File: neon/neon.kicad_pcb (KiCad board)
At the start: 2 copper layers, 42 parts, among them J1 VBUS-VCC, J2 V3V3-GND, J3 V3V3-GND, J4 V3V3-GND, J5 V3V3-VIO, Q1 BC807, Q2 BC807, Q3 BC807, Q4 BC807, Q5 BC807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

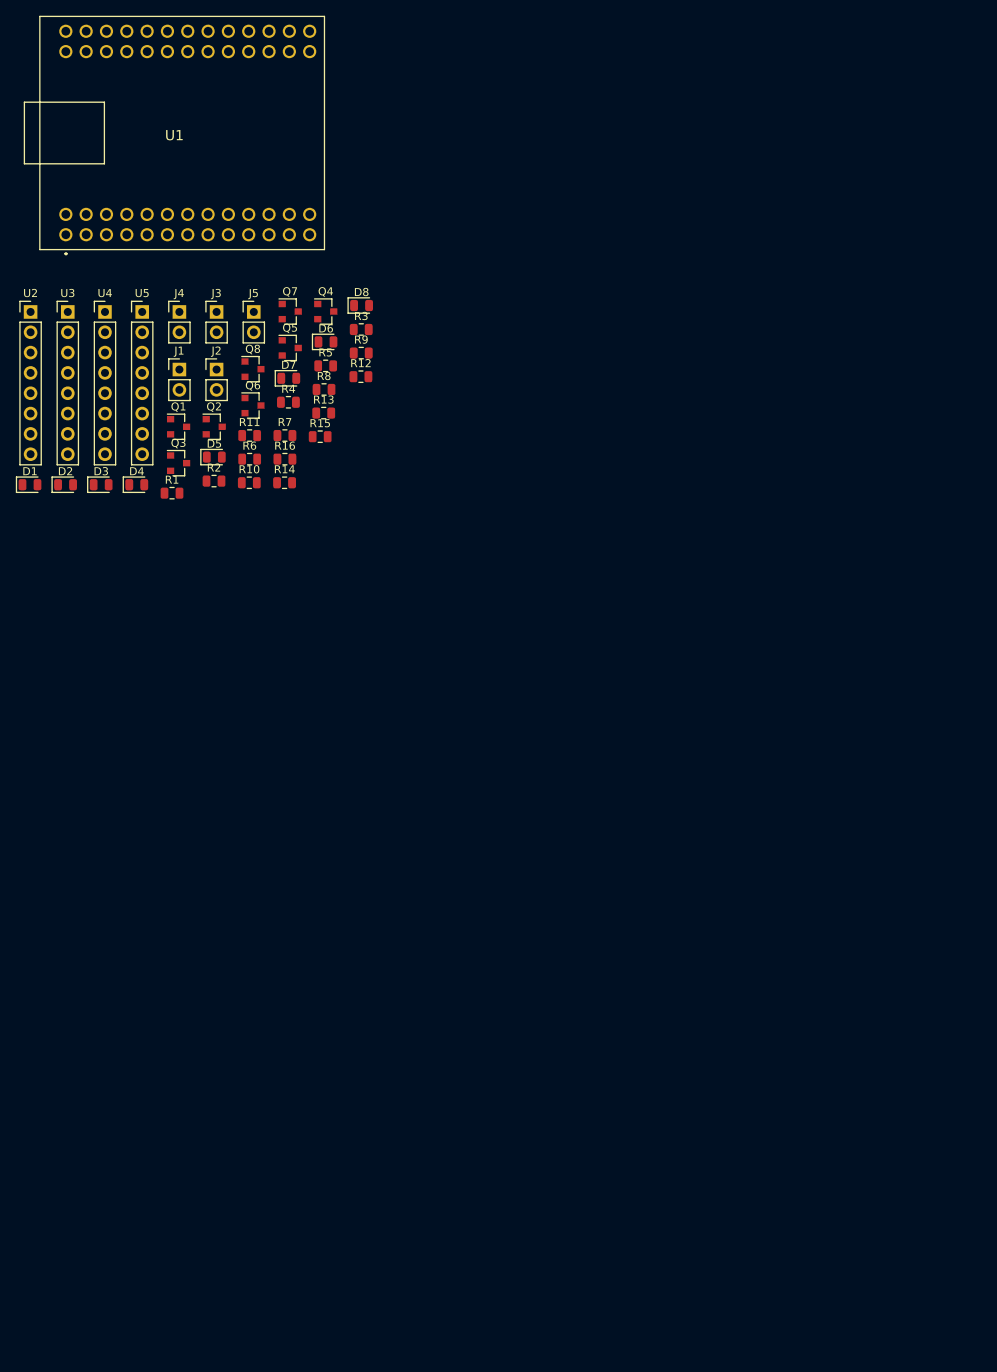
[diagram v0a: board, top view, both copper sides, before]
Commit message: Order pins on footprint - part 1
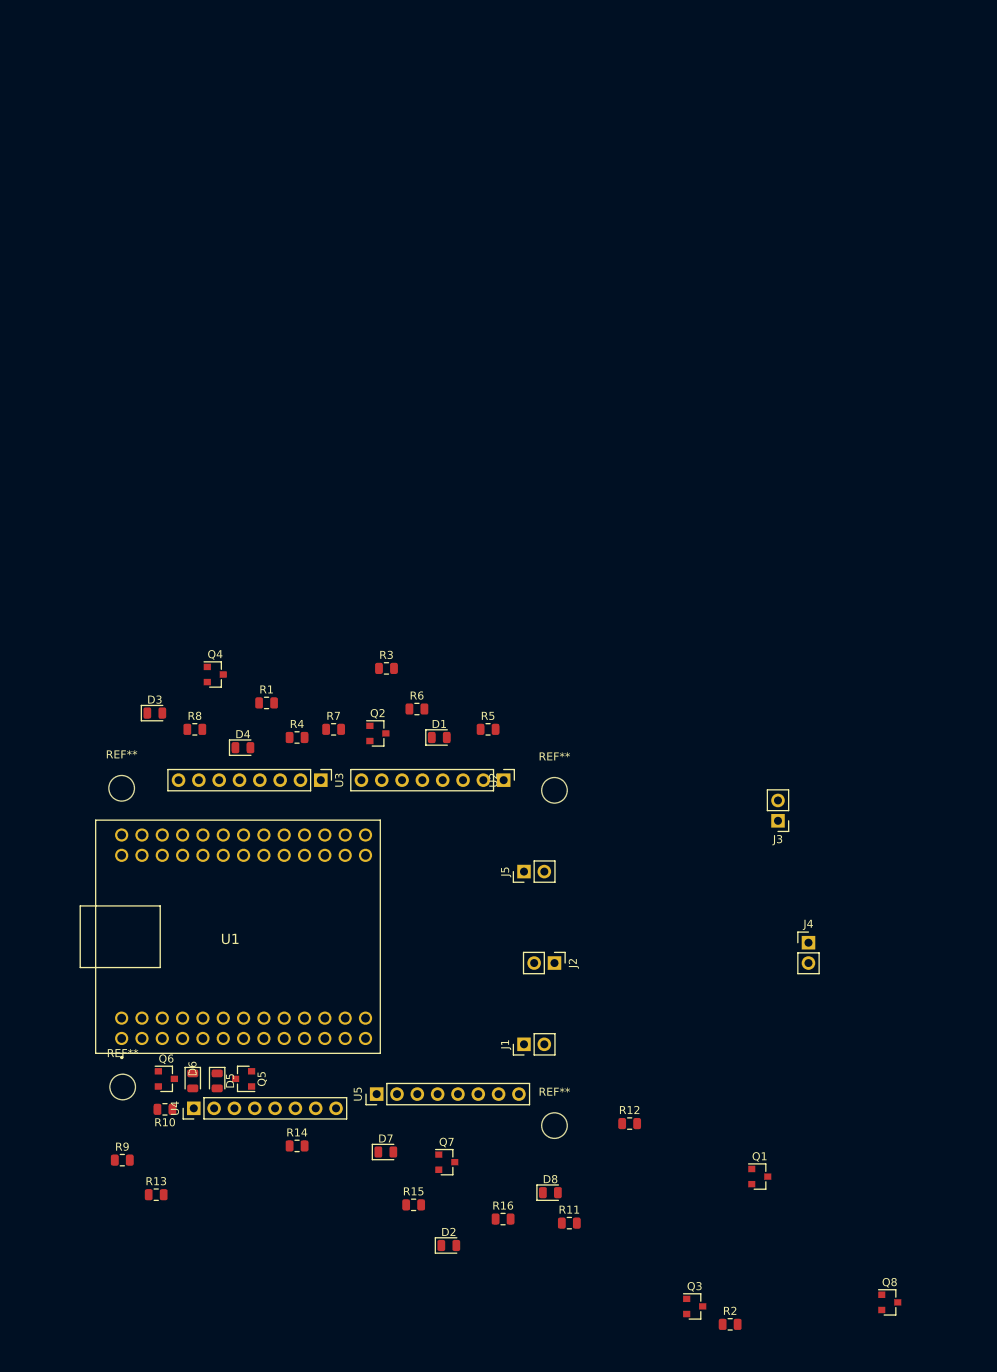
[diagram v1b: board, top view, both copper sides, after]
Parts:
- added REF**: MountingHole_3.2mm_M3, MountingHole:MountingHole_3.2mm_M3, F.Cu at (160.0, 104.1)
- added REF**: MountingHole_3.2mm_M3, MountingHole:MountingHole_3.2mm_M3, F.Cu at (160.0, 62.2)
- added REF**: MountingHole_3.2mm_M3, MountingHole:MountingHole_3.2mm_M3, F.Cu at (105.9, 62.0)
- added REF**: MountingHole_3.2mm_M3, MountingHole:MountingHole_3.2mm_M3, F.Cu at (106.0, 99.3)
- moved Q8 141.2 mm to (201.9, 126.2)
- moved Q3 123.6 mm to (177.6, 126.7)
- moved R2 123.6 mm to (182.0, 129.0)
- moved Q1 118.6 mm to (185.7, 110.5)
- moved D8 113.4 mm to (159.5, 112.5)
- moved J4 111.4 mm to (191.8, 81.3)
- moved Q7 108.1 mm to (146.6, 108.7)
- moved D2 106.5 mm to (146.8, 119.1)
- moved R11 106.2 mm to (161.9, 116.3)
- moved R9 105.2 mm to (106.0, 108.5)
- moved U5 102.1 mm to (137.8, 100.2), turned to 90 degrees
- moved U1 100.7 mm to (119.5, 80.8)
- moved U4 100.2 mm to (114.9, 102.0), turned to 90 degrees
- moved R13 99.9 mm to (110.2, 112.8)
- moved R12 99.2 mm to (169.4, 103.9)
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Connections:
- J1 pad 1: /FT4232H.sch/VBUS -> /FT4232H.sch/VCC
- J1 pad 2: (no net) -> /FT4232H.sch/VBUS
- J2 pad 1: V3V3 -> GND
- J2 pad 2: (no net) -> V3V3
- J3 pad 1: V3V3 -> GND
- J3 pad 2: (no net) -> V3V3
- J4 pad 1: V3V3 -> GND
- J4 pad 2: (no net) -> V3V3
- J5 pad 1: V3V3 -> /FT4232H.sch/VIO
- J5 pad 2: (no net) -> V3V3
- U1 pad 10: /FT4232H.sch/DD6 -> /FT4232H.sch/BD3
- U1 pad 11: /FT4232H.sch/VIO -> Net-(U1-Pad11)
- U1 pad 12: /FT4232H.sch/AD3 -> /FT4232H.sch/BD6
- U1 pad 13: /FT4232H.sch/AD5 -> Net-(U1-Pad13)
- U1 pad 14: /FT4232H.sch/AD4 -> Net-(U1-Pad14)
- U1 pad 15: /FT4232H.sch/AD7 -> Net-(U1-Pad15)
- U1 pad 16: /FT4232H.sch/AD6 -> Net-(U1-Pad16)
- U1 pad 17: /FT4232H.sch/BD1 -> Net-(U1-Pad17)
- U1 pad 18: /FT4232H.sch/BD0 -> /FT4232H.sch/AD1
- U1 pad 19: /FT4232H.sch/BD3 -> /FT4232H.sch/AD3
- U1 pad 20: /FT4232H.sch/BD2 -> /FT4232H.sch/AD4
- U1 pad 21: /FT4232H.sch/CD4 -> /FT4232H.sch/AD6
- U1 pad 22: /FT4232H.sch/BD4 -> /FT4232H.sch/BD0
- U1 pad 23: /FT4232H.sch/BD6 -> /FT4232H.sch/BD2
- U1 pad 24: /FT4232H.sch/BD5 -> /FT4232H.sch/BD4
- U1 pad 25: /FT4232H.sch/CD1 -> /FT4232H.sch/BD5
- U1 pad 27: (no net) -> /FT4232H.sch/VBUS
- U1 pad 28: (no net) -> /FT4232H.sch/VCC
- U1 pad 29: (no net) -> Net-(U1-Pad29)
- U1 pad 3: /FT4232H.sch/VCC -> Net-(U1-Pad3)
- U1 pad 30: (no net) -> Net-(U1-Pad30)
- U1 pad 31: (no net) -> /FT4232H.sch/DD7
- U1 pad 32: (no net) -> /FT4232H.sch/DD5
- U1 pad 33: (no net) -> /FT4232H.sch/DD4
- U1 pad 34: (no net) -> /FT4232H.sch/DD2
- U1 pad 35: (no net) -> /FT4232H.sch/DD0
- U1 pad 36: (no net) -> /FT4232H.sch/CD6
- U1 pad 37: (no net) -> /FT4232H.sch/CD4
- U1 pad 38: (no net) -> /FT4232H.sch/CD3
- U1 pad 39: (no net) -> /FT4232H.sch/CD1
- U1 pad 4: Net-(U1-Pad4) -> /FT4232H.sch/AD0
- U1 pad 40: (no net) -> GND
- U1 pad 41: (no net) -> Net-(U1-Pad41)
- U1 pad 42: (no net) -> Net-(U1-Pad42)
- U1 pad 43: (no net) -> Net-(U1-Pad43)
- U1 pad 44: (no net) -> /FT4232H.sch/DD6
- U1 pad 45: (no net) -> Net-(U1-Pad45)
- U1 pad 46: (no net) -> /FT4232H.sch/DD3
- U1 pad 47: (no net) -> /FT4232H.sch/DD1
- U1 pad 48: (no net) -> /FT4232H.sch/CD7
- U1 pad 49: (no net) -> /FT4232H.sch/CD5
- U1 pad 5: Net-(U1-Pad5) -> /FT4232H.sch/AD2
- U1 pad 50: (no net) -> Net-(U1-Pad50)
- U1 pad 51: (no net) -> /FT4232H.sch/CD2
- U1 pad 52: (no net) -> /FT4232H.sch/CD0
- U1 pad 6: Net-(U1-Pad6) -> /FT4232H.sch/VIO
- U1 pad 7: /FT4232H.sch/AD0 -> /FT4232H.sch/AD5
- U1 pad 8: Net-(U1-Pad8) -> /FT4232H.sch/AD7
- U1 pad 9: /FT4232H.sch/AD2 -> /FT4232H.sch/BD1
- U2 pad 1: /FT4232H.sch/CD1 -> /FT4232H.sch/CD0
- U2 pad 2: /FT4232H.sch/CD2 -> /FT4232H.sch/CD1
- U2 pad 3: /FT4232H.sch/CD3 -> /FT4232H.sch/CD2
- U2 pad 4: /FT4232H.sch/CD4 -> /FT4232H.sch/CD3
- U2 pad 5: /FT4232H.sch/CD5 -> /FT4232H.sch/CD4
- U2 pad 6: /FT4232H.sch/CD6 -> /FT4232H.sch/CD5
- U2 pad 7: /FT4232H.sch/CD7 -> /FT4232H.sch/CD6
- U2 pad 8: (no net) -> /FT4232H.sch/CD7
- U3 pad 1: /FT4232H.sch/DD1 -> /FT4232H.sch/DD0
- U3 pad 2: /FT4232H.sch/DD2 -> /FT4232H.sch/DD1
- U3 pad 3: /FT4232H.sch/DD3 -> /FT4232H.sch/DD2
- U3 pad 4: /FT4232H.sch/DD4 -> /FT4232H.sch/DD3
- U3 pad 5: /FT4232H.sch/DD5 -> /FT4232H.sch/DD4
- U3 pad 6: /FT4232H.sch/DD6 -> /FT4232H.sch/DD5
- U3 pad 7: /FT4232H.sch/DD7 -> /FT4232H.sch/DD6
- U3 pad 8: (no net) -> /FT4232H.sch/DD7
- U4 pad 1: /FT4232H.sch/AD1 -> /FT4232H.sch/AD0
- U4 pad 2: /FT4232H.sch/AD2 -> /FT4232H.sch/AD1
- U4 pad 3: /FT4232H.sch/AD3 -> /FT4232H.sch/AD2
- U4 pad 4: /FT4232H.sch/AD4 -> /FT4232H.sch/AD3
- U4 pad 5: /FT4232H.sch/AD5 -> /FT4232H.sch/AD4
- U4 pad 6: /FT4232H.sch/AD6 -> /FT4232H.sch/AD5
- U4 pad 7: /FT4232H.sch/AD7 -> /FT4232H.sch/AD6
- U4 pad 8: (no net) -> /FT4232H.sch/AD7
- U5 pad 1: /FT4232H.sch/BD1 -> /FT4232H.sch/BD0
- U5 pad 2: /FT4232H.sch/BD2 -> /FT4232H.sch/BD1
- U5 pad 3: /FT4232H.sch/BD3 -> /FT4232H.sch/BD2
- U5 pad 4: /FT4232H.sch/BD4 -> /FT4232H.sch/BD3
- U5 pad 5: /FT4232H.sch/BD5 -> /FT4232H.sch/BD4
- U5 pad 6: /FT4232H.sch/BD6 -> /FT4232H.sch/BD5
- U5 pad 7: /FT4232H.sch/BD7 -> /FT4232H.sch/BD6
- U5 pad 8: (no net) -> /FT4232H.sch/BD7
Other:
- net class Default: clearance 0.2 -> 0.127; trace_width 0.25 -> 0.127
- rule trace_clearance: 0.2 -> 0.127
- rule trace_min: 0.2 -> 0.1

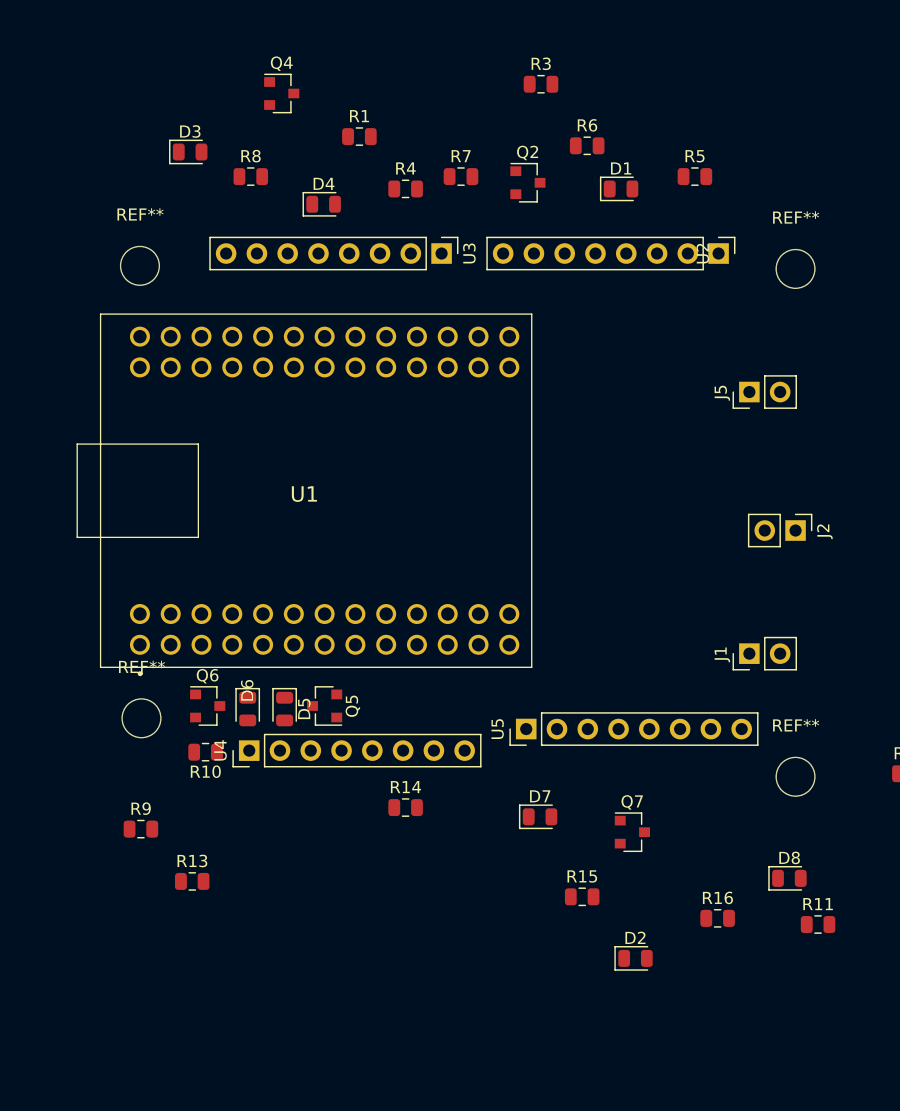
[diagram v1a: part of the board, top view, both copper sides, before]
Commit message: Order pins on footprint - part 2
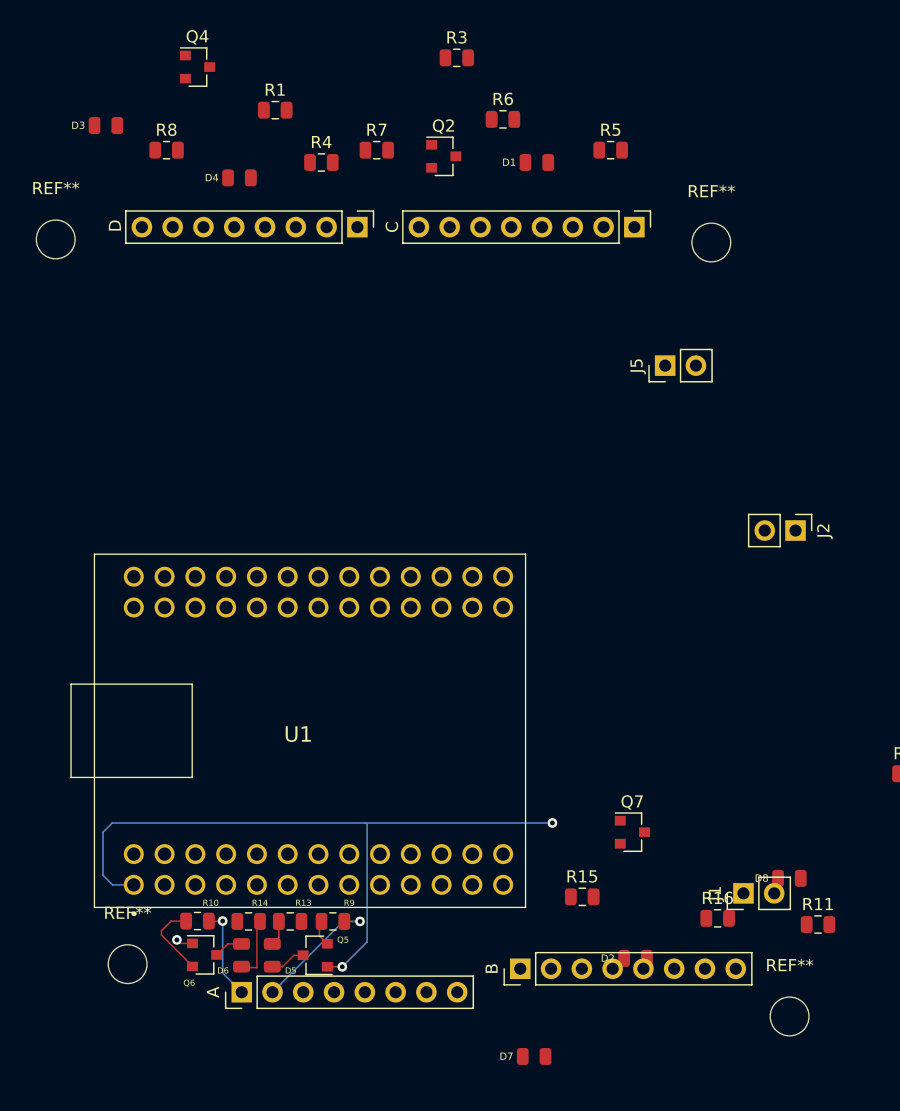
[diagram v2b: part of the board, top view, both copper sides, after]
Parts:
- removed the REF** at (160.0, 104.1)
- removed the REF** at (160.0, 62.2)
- removed the REF** at (105.9, 62.0)
- added REF**: MountingHole_3.2mm_M3, MountingHole:MountingHole_3.2mm_M3, F.Cu at (159.5, 123.9)
- added REF**: MountingHole_3.2mm_M3, MountingHole:MountingHole_3.2mm_M3, F.Cu at (153.1, 60.0)
- added REF**: MountingHole_3.2mm_M3, MountingHole:MountingHole_3.2mm_M3, F.Cu at (99.0, 59.8)
- D1, D2, D3, D4, D5, D6, D7, D8: footprint LED_SMD:LED_0805_2012Metric -> neon_footprints:LED_0805_2012Metric
- U1: footprint neon_footprints:FT4232H-MINI-MODULE -> neon_footprints:FT4232H-MINI-MODULE-2
- moved Q5 20.6 mm to (120.4, 118.9)
- moved Q6 20.5 mm to (111.3, 118.8)
- moved D5 20.3 mm to (116.8, 118.9)
- moved D6 20.3 mm to (114.3, 118.9), turned to 90 degrees
- moved REF** 20.3 mm to (104.9, 119.6)
- moved A 19.9 mm to (114.3, 121.9)
- moved U1 19.8 mm to (119.0, 100.7)
- moved B 19.8 mm to (137.3, 120.0)
- moved D7 19.8 mm to (138.4, 127.2)
- moved J1 19.8 mm to (155.7, 113.8)
- moved R9 17.6 mm to (121.8, 116.1), turned to 180 degrees
- moved R14 16.0 mm to (114.9, 116.1)
- moved R10 14.0 mm to (110.7, 116.0)
- moved R13 8.73 mm to (118.3, 116.1), turned to 180 degrees
- moved J5 7.28 mm to (149.3, 70.2)
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- renumbered U4 to A, U5 to B, U2 to C, U3 to D
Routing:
- net V3V3: track 0.00 -> 59.2 mm, vias 0 -> 3
- net /FT4232H.sch/AD1: track 0.00 -> 10.9 mm, vias 0 -> 1
- net /FT4232H.sch/AD0: track 0.00 -> 7.67 mm, vias 0 -> 1
- net Net-(Q6-Pad2): track 0.00 -> 6.60 mm
- net Net-(D6-Pad1): track 0.00 -> 5.16 mm
- net Net-(D5-Pad2): track 0.00 -> 3.04 mm
- net Net-(D6-Pad2): track 0.00 -> 2.42 mm
- net Net-(D5-Pad1): track 0.00 -> 2.19 mm
- net Net-(Q5-Pad2): track 0.00 -> 2.11 mm

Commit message: Board cuts - part 1
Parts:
- removed J1: VBUS-VCC, Connector_PinHeader_2.54mm:PinHeader_1x02_P2.54mm_Vertical
- moved J3 51.8 mm to (146.1, 96.5), turned to 270 degrees
- moved J4 51.7 mm to (146.1, 105.4), turned to 270 degrees
- moved Q7 27.2 mm to (173.0, 114.9)
- moved J2 22.1 mm to (146.1, 101.0)
- moved J5 22.1 mm to (146.1, 92.1), turned to 270 degrees
- moved B 4.98 mm to (132.7, 121.9)
- moved A 3.83 mm to (110.5, 121.9)
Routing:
- net V3V3: track 59.2 -> 89.6 mm
- net /FT4232H.sch/AD1: track 10.9 -> 14.7 mm
- net /FT4232H.sch/VBUS: track 0.00 -> 3.61 mm, vias 0 -> 1
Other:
- board outline added: 52.7 x 49.5 mm
